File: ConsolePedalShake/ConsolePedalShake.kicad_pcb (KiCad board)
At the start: 2 copper layers, 100 x 60 mm, 45 parts, among them J1 Conn_02x25_Counter_Clockwise, J2 JP1, Q1 2N5088, Q2 2N5088, Q3 2N5088, Q4 2N5088, SW1 Speed

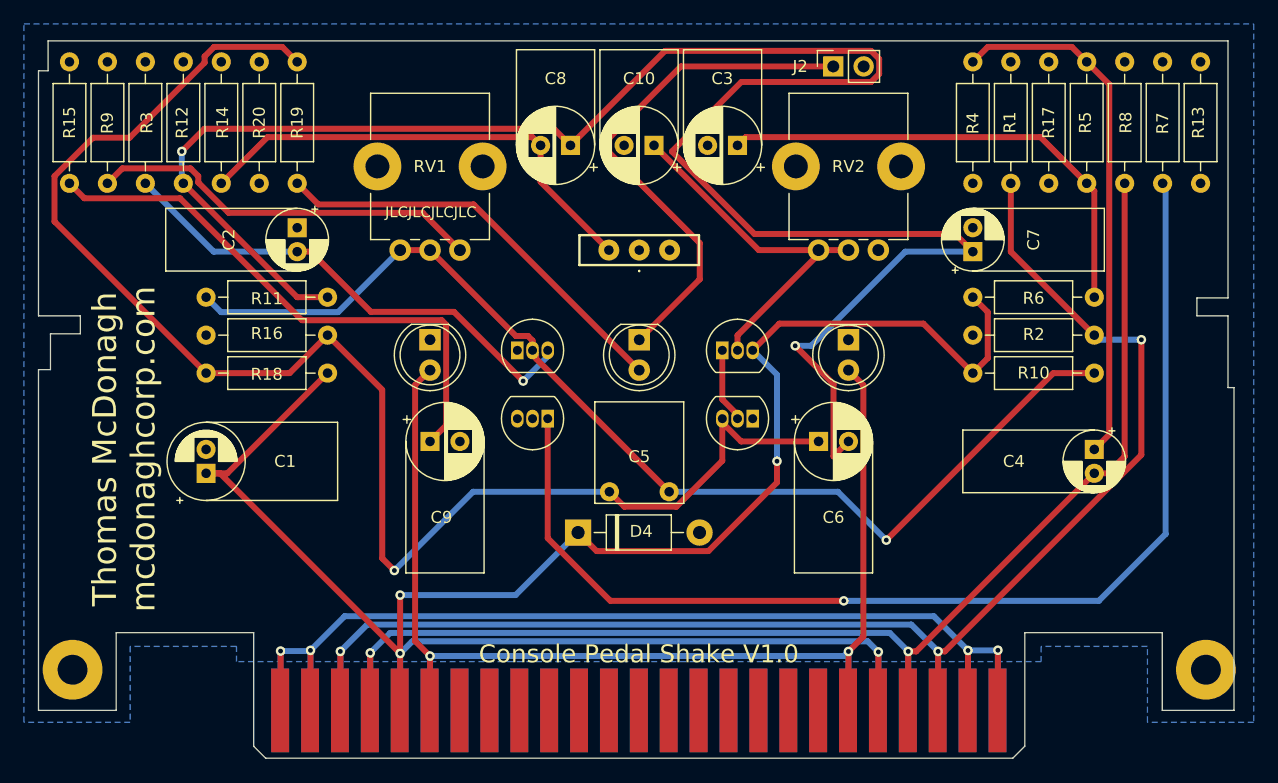
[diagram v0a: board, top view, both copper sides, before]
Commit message: Finalized new pedal based on Vanilla Shake by diyguitarpedals.com.au
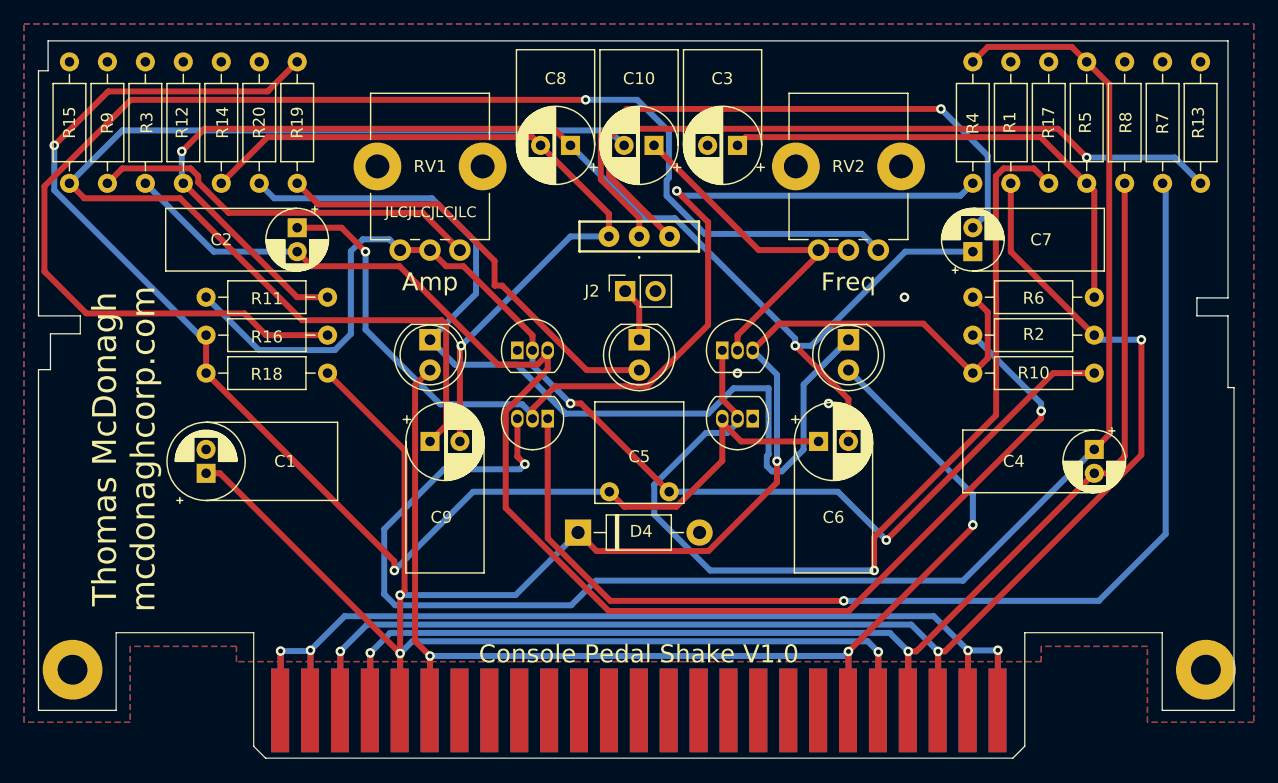
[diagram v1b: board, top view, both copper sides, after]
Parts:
- moved J2 25.6 mm to (131.6, 90.9)
- moved R16 10.2 mm to (106.7, 94.6), turned to 180 degrees
- moved SW1 1.14 mm to (132.8, 86.4)
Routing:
- net Net-(R16-Pad1): track 0.00 -> 114.4 mm, vias 0 -> 1
- net Net-(C4-Pad1): track 44.3 -> 133.0 mm, vias 0 -> 1
- net Net-(C2-Pad1): track 0.00 -> 86.4 mm, vias 0 -> 2
- net Net-(D1-Pad1): track 0.54 -> 83.0 mm
- net Net-(C2-Pad2): track 42.0 -> 119.6 mm
- net Net-(Q3-Pad1): track 6.24 -> 81.0 mm, vias 0 -> 1
- net Net-(R13-Pad1): track 0.00 -> 62.0 mm, vias 0 -> 1
- net Net-(C6-Pad2): track 162.4 -> 106.7 mm
- net Net-(C7-Pad2): track 0.00 -> 51.3 mm, vias 0 -> 1
- net Net-(C10-Pad2): track 46.7 -> 95.5 mm
- net Net-(D3-Pad1): track 43.3 -> 4.56 mm
- net Net-(C8-Pad2): track 39.7 -> 62.8 mm, vias 0 -> 1
- net Net-(C5-Pad2): track 125.6 -> 115.7 mm, vias 1 -> 2
- net Net-(C5-Pad1): track 93.5 -> 101.7 mm, vias 1 -> 2
- net +9V: track 178.1 -> 185.9 mm
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- added copper zone on F.Cu, net GND
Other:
- board text added: "Amp"
- board text added: "Freq"
